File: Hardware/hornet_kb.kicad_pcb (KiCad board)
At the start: 4 copper layers, 193 x 100.3 mm, 150 parts, among them J1 Conn_ST_STDC14, J10 USB_C_Receptacle_USB2.0, J2 Conn_01x03, SW1 ESC, SW10 TAB, SW11 Q, SW12 W, SW13 E, SW14 R, SW15 T, SW17 M1, SW18 CAPS, SW19 A, SW2 `, SW20 S, SW21 D, SW22 F, SW23 G, SW25 M2, SW26 M3, SW27 SW_DPDT_x2, SW28 SHIFT, SW29 CTRL, SW3 1, SW30 Rot_Enc, SW31 Z, SW32 WIN, SW34 X, SW35 FN, SW37 C, SW38 ALT, SW4 2, SW40 V, SW41 SPACE, SW43 B, SW44 DEL, SW5 3, SW6 4, SW7 5, SW8 6, SW9 M0, SW98 SW_Push, U1 nRF52840, U2 BQ24040, U3 BQ51050BRHL, U4 AP22814BW5, U5 TPS2116DRL, Y1 32.768kHz, Y3 Crystal_GND24

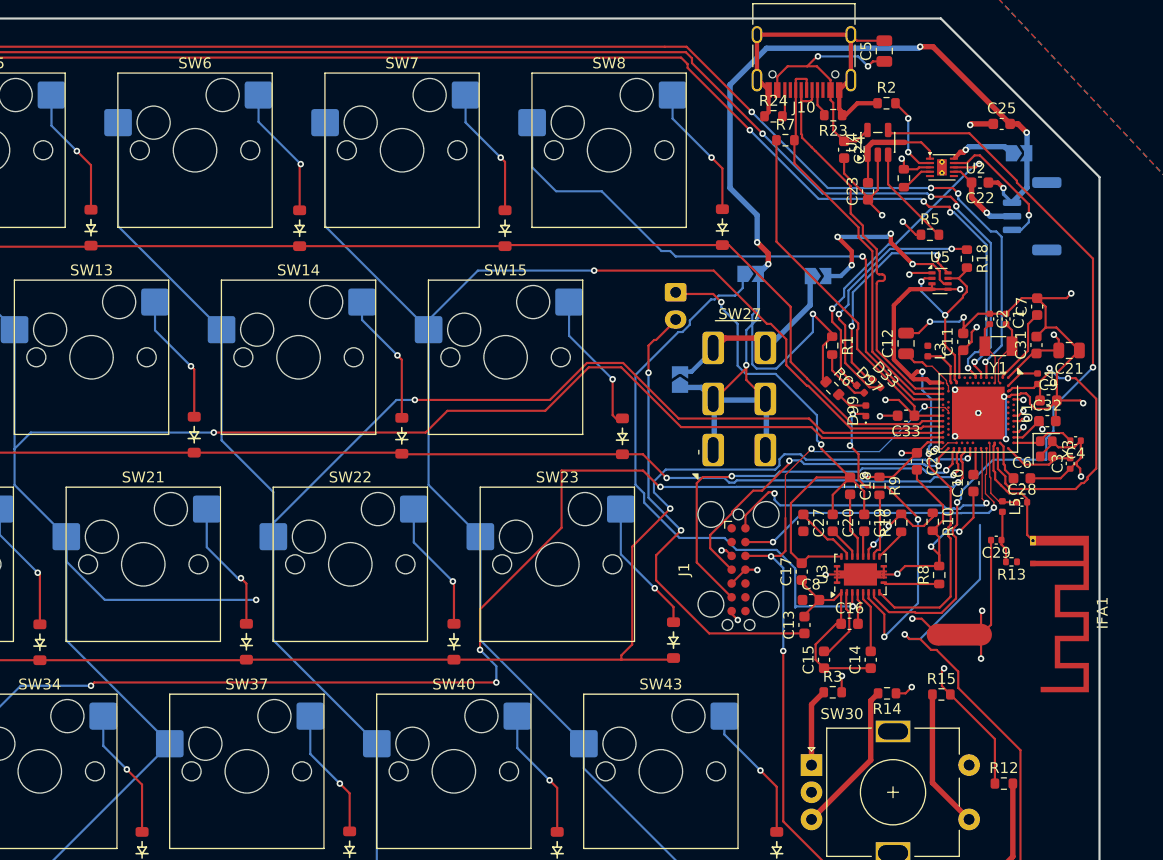
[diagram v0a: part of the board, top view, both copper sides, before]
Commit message: Resolving DRC errors
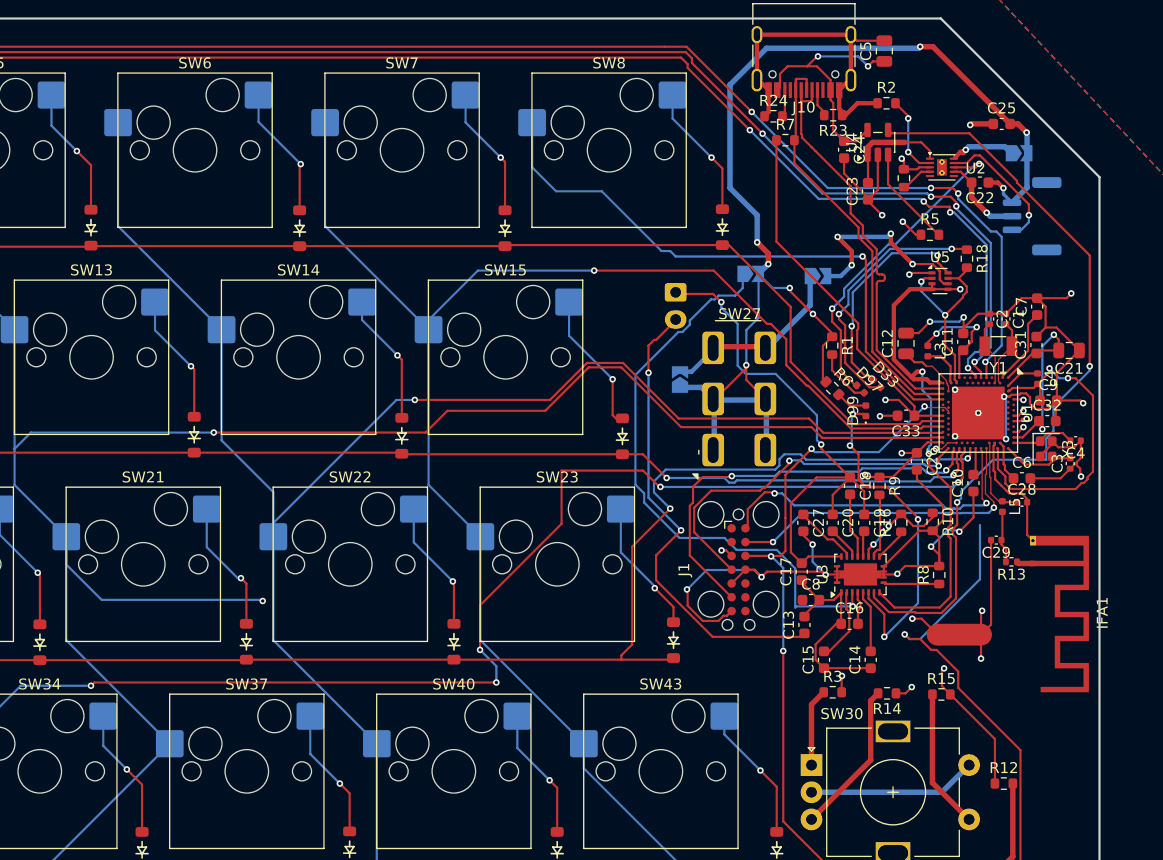
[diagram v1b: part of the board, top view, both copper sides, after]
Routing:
- net GND: track 182.1 -> 228.9 mm, vias 24 -> 25
- net VDD: track 80.1 -> 94.6 mm, vias 10 -> 11
- net +BATT: track 121.7 -> 111.0 mm, vias 7 -> 8
- net /Rotary_SW: track 63.5 -> 57.7 mm
- net /PRC_DIO: track 30.3 -> 33.8 mm
- net /R_ROW_3: track 213.3 -> 215.0 mm
- net Net-(IFA1-ANT): track 0.00 -> 1.53 mm
- net /R_COL_4: track 203.5 -> 204.3 mm
- net Net-(JP1-A): track 18.0 -> 17.4 mm
- net /PRG_CLK: track 37.9 -> 38.5 mm

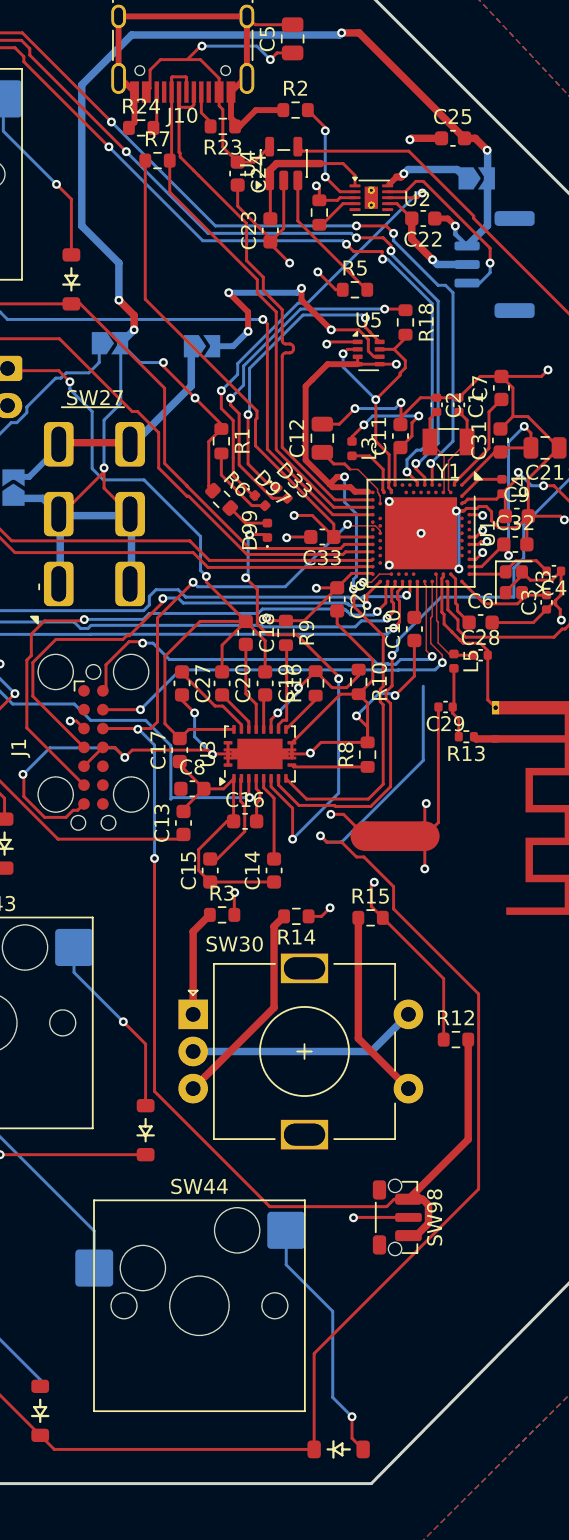
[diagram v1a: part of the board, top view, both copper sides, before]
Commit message: Change reset switchto custom footprint
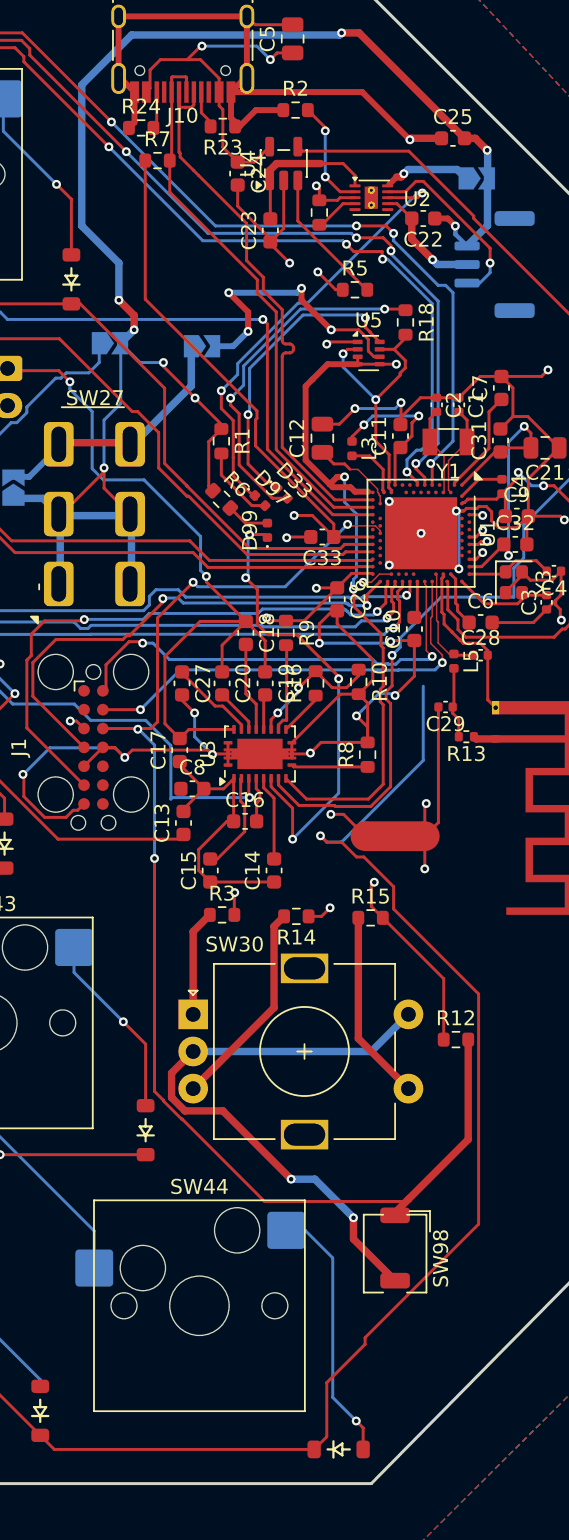
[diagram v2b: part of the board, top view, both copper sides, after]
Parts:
- SW98: footprint Button_Switch_SMD:SW_Push_1P1T-MP_NO_Horizontal_Alps_SKRTLAE010 -> ScottoKeebs_Miscellaneous:SW_DIP_SPSTx01_Slide_6.7x4.1mm_W6.73mm_P2.54mm_LowProfile_JPin
- moved SW98 0.14 mm to (217.6, 127.3)
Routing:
- net GND: track 228.9 -> 272.6 mm, vias 25 -> 28
- net /~{RESET}: track 91.4 -> 88.1 mm
- net Net-(D44-A): track 16.9 -> 17.6 mm

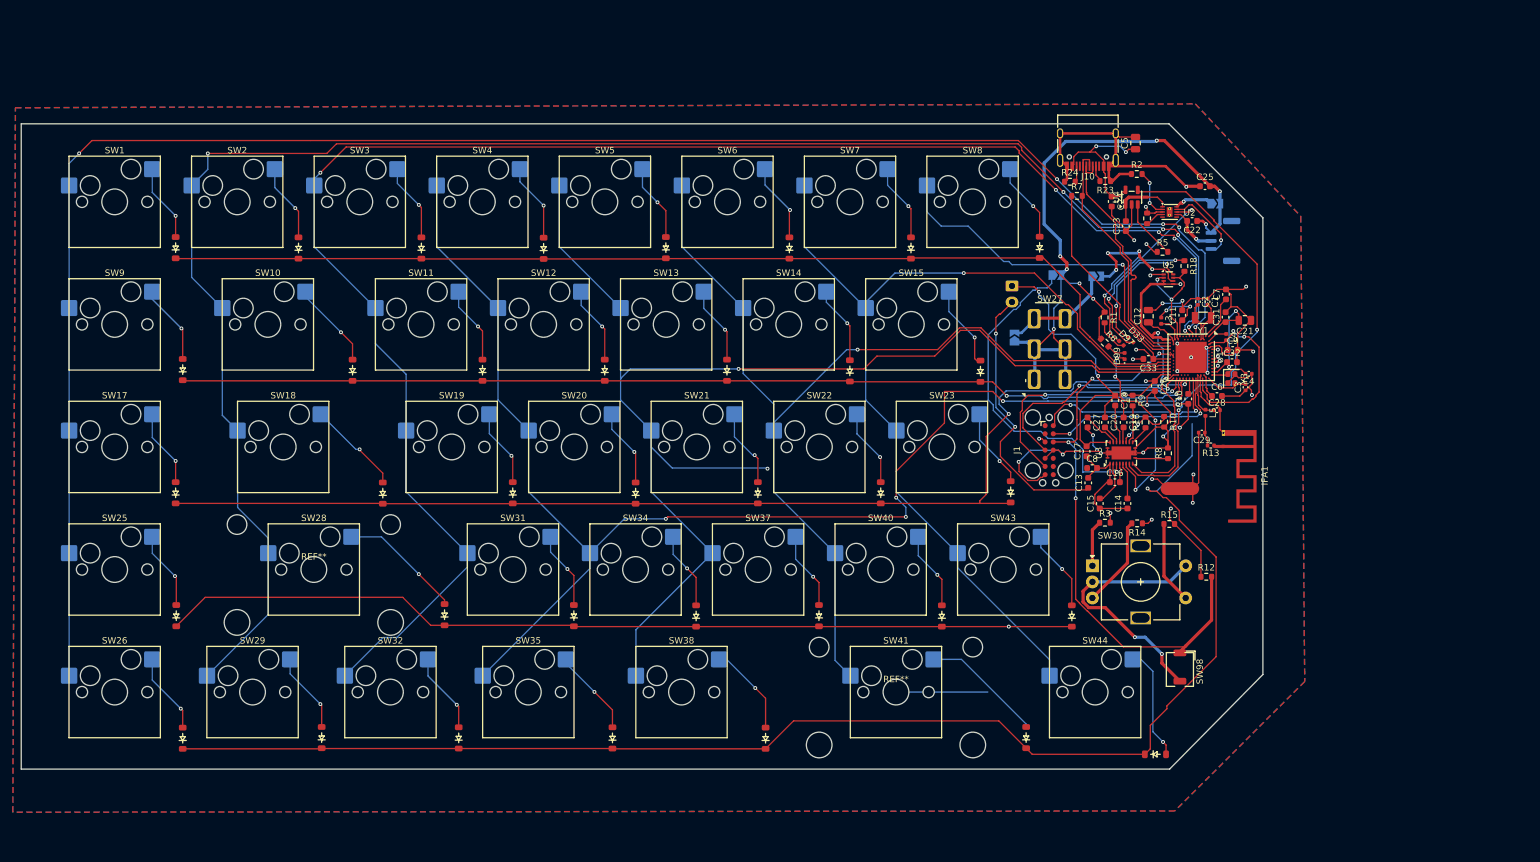
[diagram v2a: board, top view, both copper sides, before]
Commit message: added mounting holes
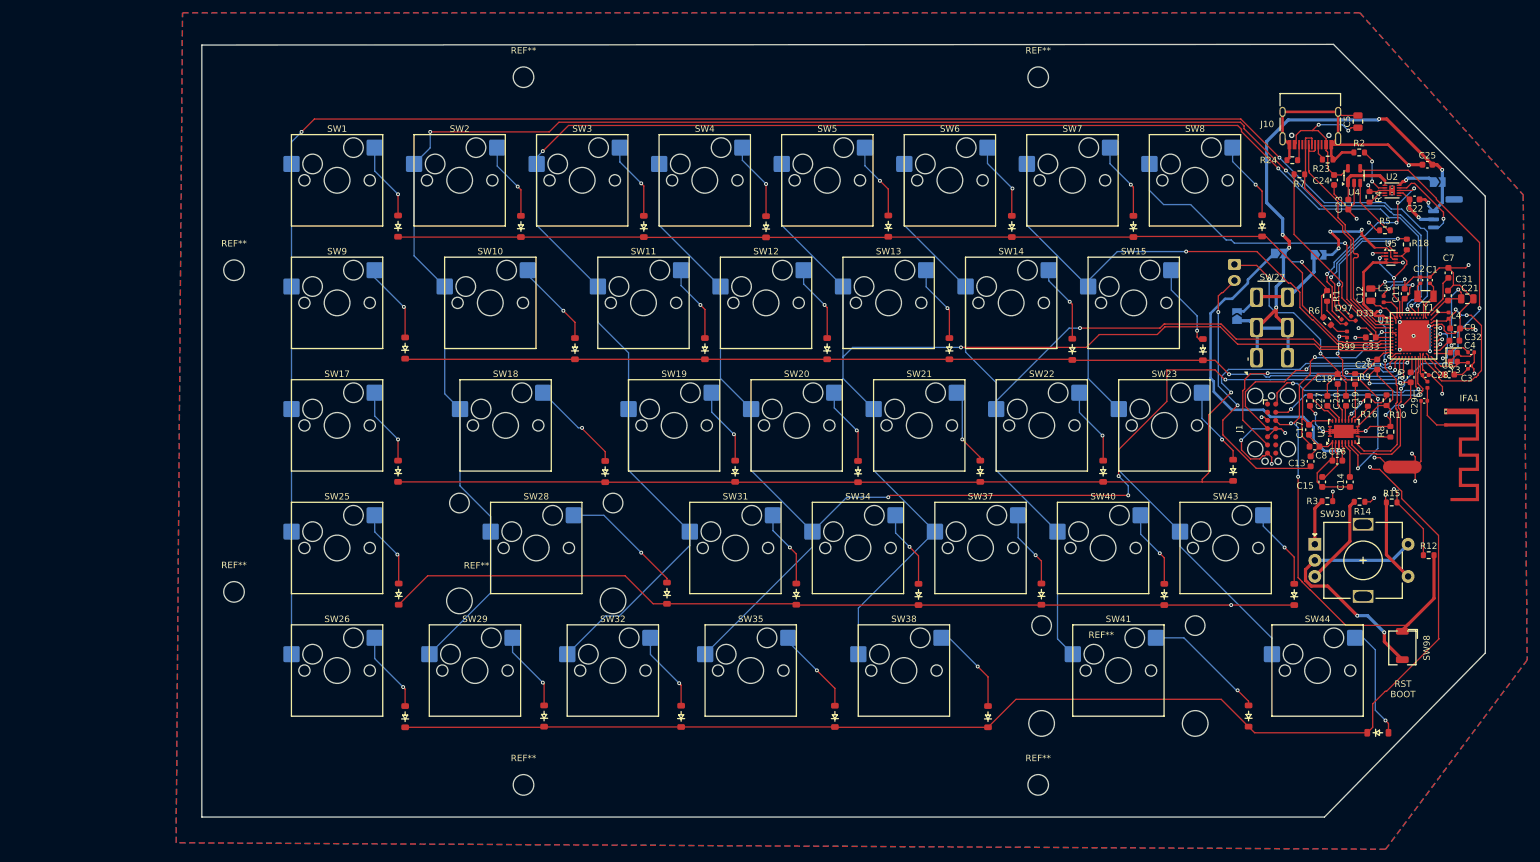
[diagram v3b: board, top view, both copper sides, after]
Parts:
- removed R13: 0, Resistor_SMD:R_0402_1005Metric
- added REF**: MountingHole_3.2mm_M3, MountingHole:MountingHole_3.2mm_M3, F.Cu at (70.6, 117.8)
- added REF**: MountingHole_3.2mm_M3, MountingHole:MountingHole_3.2mm_M3, F.Cu at (195.6, 37.8)
- added REF**: MountingHole_3.2mm_M3, MountingHole:MountingHole_3.2mm_M3, F.Cu at (195.6, 147.8)
- added REF**: MountingHole_3.2mm_M3, MountingHole:MountingHole_3.2mm_M3, F.Cu at (115.6, 37.8)
- added REF**: MountingHole_3.2mm_M3, MountingHole:MountingHole_3.2mm_M3, F.Cu at (115.6, 147.8)
- added REF**: MountingHole_3.2mm_M3, MountingHole:MountingHole_3.2mm_M3, F.Cu at (70.6, 67.8)
- C1, C2, C3, C4: value 12pF -> 12p
- C10: value 820pF -> 820p
- C11, C26, C31, C32, C33, C6, C8: value 100pF -> 100p
- C12, C21, C27, C5: value 4.7uF -> 4.7u
- C13: value 200nF -> 200n
- C14, C19: value 22nF -> 22n
- C15, C20: value 10nF -> 10n
- C16, C18: value 470pF -> 470p
- C17: value 2.2nF -> 2.2n
- C22, C23, C9: value 1uF -> 1u
- C24, C25: value 10uF -> 10u
- C28, C29: value 1pF -> 1p
- C7: value 100nF -> 100n
- JP4: value PWR_SWITCH -> ~{PWR_SWITCH}
- L1: value 6.3uH -> 6.3u
- L3: value 10uH -> 10u
- L4: value 25uH -> 25u
- L5: value 4.7nH -> 4.7n
- moved C6 36.3 mm to (259.5, 84.0)
- moved C29 34.9 mm to (255.6, 88.1)
- moved L5 34.8 mm to (256.1, 85.6)
- moved C15 34.7 mm to (239.8, 100.7)
- moved C16 34.7 mm to (242.1, 97.4)
- moved C22 34.7 mm to (254.1, 56.8)
- moved C24 34.7 mm to (241.6, 53.8)
- moved C25 34.7 mm to (256.1, 51.4)
- moved C3 34.7 mm to (262.4, 82.6)
- moved C4 34.7 mm to (262.9, 80.5)
- moved C9 34.7 mm to (260.4, 76.8)
- moved D19 34.7 mm to (148.5, 99.0)
- moved D20 34.7 mm to (167.6, 99.1)
- moved D21 34.7 mm to (186.6, 99.0)
- moved D31 34.7 mm to (158.0, 118.1)
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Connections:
- C29 pad 1: Net-(C29-Pad1) -> Net-(IFA1-ANT)
- L5 pad 2: Net-(C29-Pad1) -> Net-(IFA1-ANT)
- U2 pad 11: (no net) -> GND
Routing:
- net /R_COL_4: track 204.3 -> 180.0 mm, vias 2 -> 1
- net GND: track 272.6 -> 251.8 mm, vias 28 -> 29
- net /R_ROW_4: track 243.0 -> 226.1 mm
- net /Rotary_SW: track 57.7 -> 47.2 mm, vias 1 -> 3
- net Net-(IFA1-ANT): track 1.53 -> 7.81 mm
- net Net-(U3-AC2): track 51.5 -> 56.4 mm
- net Net-(C29-Pad1): track 4.81 -> 0.00 mm
- net /ANT: track 7.42 -> 4.87 mm
- net /R_COL_5: track 158.7 -> 156.5 mm
- net VSS_PA: track 24.7 -> 23.1 mm, vias 2 -> 3
- net VDD: track 94.6 -> 92.9 mm
- net /Rotary_L: track 51.7 -> 50.2 mm
- net Net-(D97-K): track 30.4 -> 31.8 mm, vias 2 -> 4
- net Net-(D21-A): track 12.2 -> 10.9 mm
- net /R_COL_2: track 265.9 -> 264.6 mm, vias 5 -> 3
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- added copper zone on In1.Cu, net GND
- added copper zone on In2.Cu, net VBUS
- added copper zone on In1.Cu, net VSS_PA
- removed copper zone on In2.Cu, net GND
- removed copper zone on In1.Cu, net VBUS
- removed copper zone on In1.Cu, net VDD
- removed copper zone on In2.Cu, net VSS_PA
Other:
- board size 193 x 100.3 mm -> 199.5 x 120.1 mm
- board text added: "RST BOOT"
